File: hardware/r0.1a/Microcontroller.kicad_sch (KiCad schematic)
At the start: 77 parts, among them J1 STLink, J2 USB_C, J3 OLED, SW1 Button Up, SW2 Button Down, SW3 Reset, SW4 Button Green, SW5 Button Left, SW6 Button Red, SW7 Button Right, U1 STM32F407VETx, U2 LM1117-3.3, U3 USBLC6-2, U4 W25Q16, X1 12 MHz TCXO, Y1 8 MHz

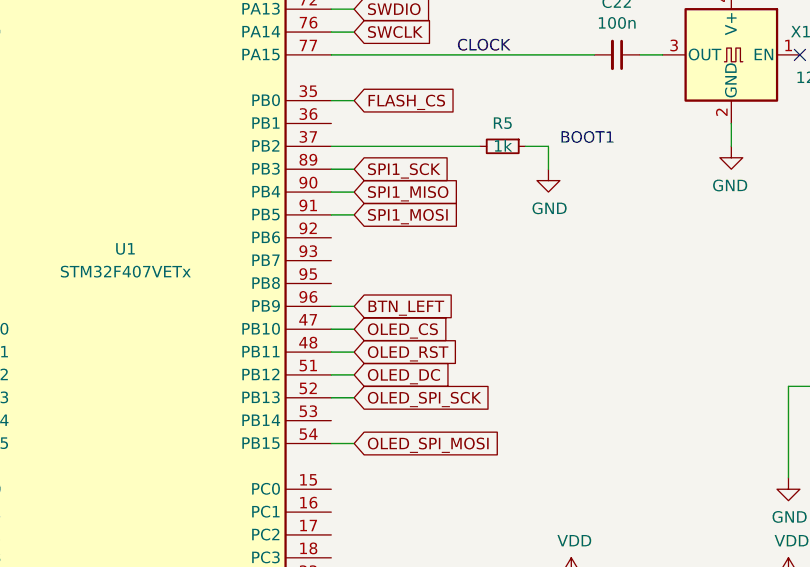
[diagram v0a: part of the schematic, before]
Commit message: Added RTC
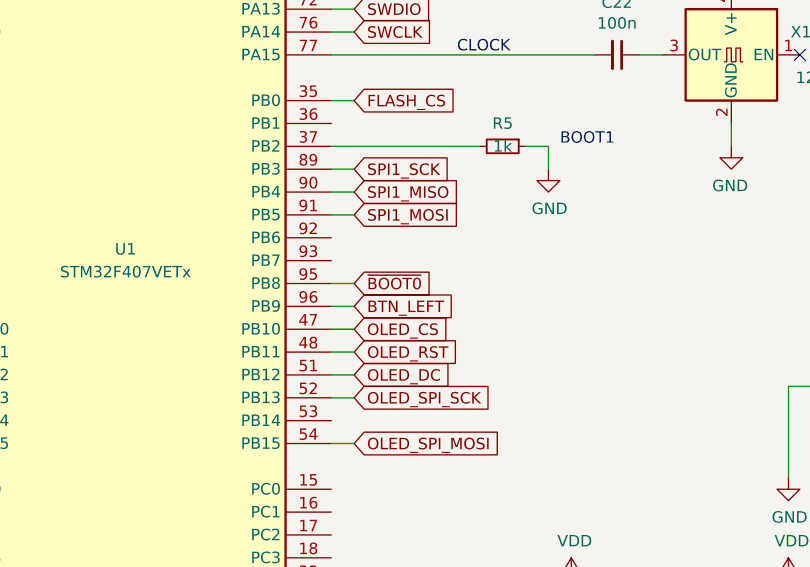
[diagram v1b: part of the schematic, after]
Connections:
- net ~{BOOT0}: now also U1.95 (PB8)
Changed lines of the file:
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@@
+    (stroke (width 0) (type solid) (color 0 0 0 0))
+  )
+  (wire (pts (xy 118.11 97.79) (xy 120.65 97.79))
     (stroke (width 0) (type solid) (color 0 0 0 0))
   )
@@
       (effects (font (size 1.27 1.27)) hide)
     )
+  )
+  (global_label "~{BOOT0}" (shape input) (at 120.65 97.79 0) (fields_autoplaced)
+    (effects (font (size 1.27 1.27)) (justify left))
+    (property "Intersheet References" "${INTERSHEET_REFS}" (id 0) (at 190.5 137.16 0)
+      (effects (font (size 1.27 1.27)) hide)
+    )
